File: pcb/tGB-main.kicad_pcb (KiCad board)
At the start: 2 copper layers, 51 x 61 mm, 69 parts, among them J1 DMG-CardEdge, J2 PROG_PORT, Q1 DMG3415U, Q2 HN4A56JU, Q3 2N7002K, U1 TC74LCXR163245FT, U2 TC74LCXR163245FT, U3 ICE40UP5K-SG48ITR, U4 TPS79901DDCR, U5 TPS79901DDCR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

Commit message: rename project
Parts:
- J1: value DMG-CardEdge -> GB-CardEdge; footprint DMG-CardEdge:DMG-CardEdge -> GB-CardEdge:GB-CardEdge
- J2: footprint pinheader:pinheader-10p-sm -> PinHeader:PinHeader-10P-Sidemount

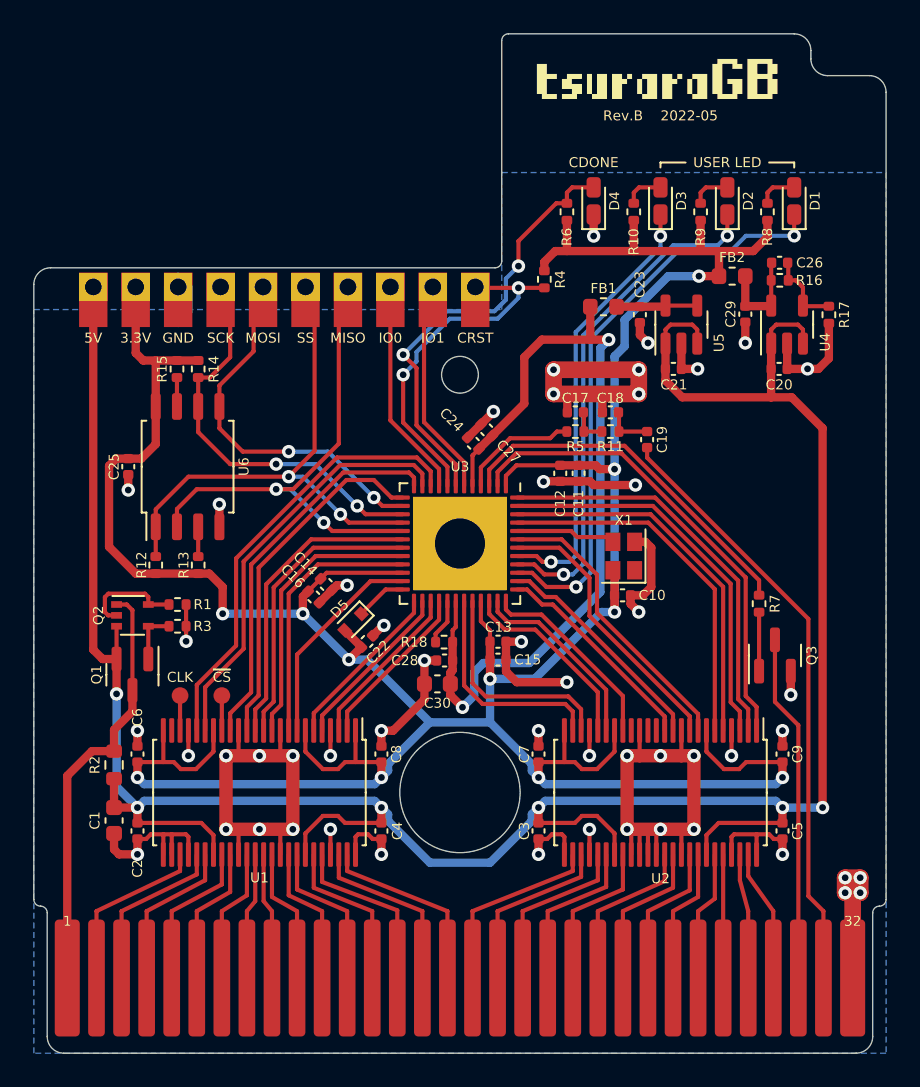
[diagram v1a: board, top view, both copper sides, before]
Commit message: rename project, update pcb
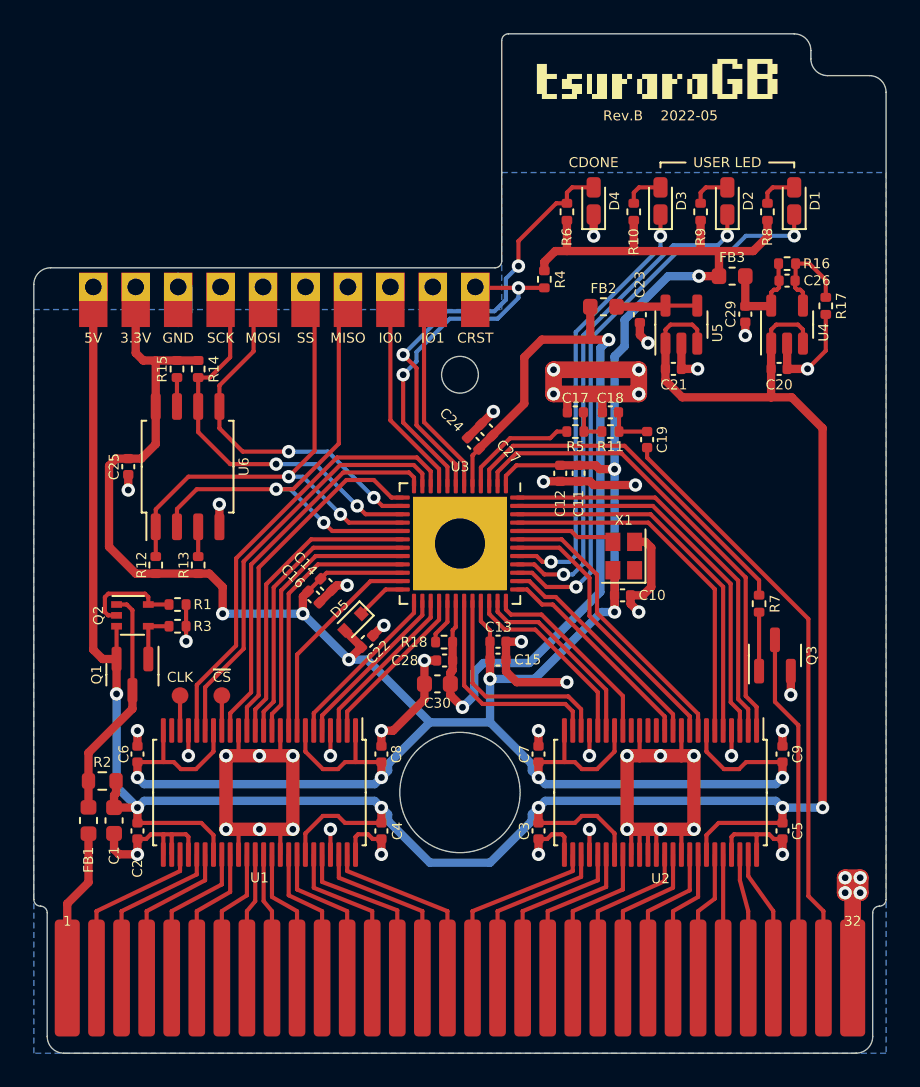
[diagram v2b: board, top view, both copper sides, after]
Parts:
- added FB1: MPZ1608S601ATA00, Inductor_SMD:L_0603_1608Metric, F.Cu at (37.8, 81.6)
- moved R2 1.19 mm to (38.6, 79.2), turned to 0 degrees
- moved C26 1.16 mm to (79.6, 49.3)
- moved R16 1.09 mm to (79.6, 48.2)
- moved R17 0.56 mm to (81.9, 50.8)
- renumbered FB1 to FB2, FB2 to FB3
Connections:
- Q1 pad 3: /VCC -> /VCC0
- Q2 pad 1: /VCC -> /VCC0
- R2 pad 1: /VCC -> /VCC0
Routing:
- net /VCC: track 25.5 -> 9.16 mm
- net /VCC0: track 0.00 -> 14.0 mm
- net Net-(C26-Pad2): track 4.77 -> 6.08 mm

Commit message: update R16,R17 value
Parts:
- R16: value 100kΩ -> 120kΩ
- R17: value 56kΩ -> 68kΩ
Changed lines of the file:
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@@
     (grid_origin 34.5 95.5)
     (pcbplotparams
-      (layerselection 0x00010f0_ffffffff)
+      (layerselection 0x00010fc_ffffffff)
       (disableapertmacros false)
       (usegerberextensions false)
@@
     (fp_line (start -2.5 -3.5) (end 3.5 -3.5) (layer "F.Fab") (width 0.1))
     (fp_line (start -3.5 -2.5) (end -2.5 -3.5) (layer "F.Fab") (width 0.1))
-    (pad "" smd roundrect (at -2.1 -0.7 270) (size 1.13 1.13) (layers "F.Paste") (roundrect_rratio 0.221239))
-    (pad "" smd roundrect (at 2.1 2.1 270) (size 1.13 1.13) (layers "F.Paste") (roundrect_rratio 0.221239))
-    (pad "" smd roundrect (at 0.7 -2.1 270) (size 1.13 1.13) (layers "F.Paste") (roundrect_rratio 0.221239))
-    (pad "" smd roundrect (at -2.1 0.7 270) (size 1.13 1.13) (layers "F.Paste") (roundrect_rratio 0.221239))
-    (pad "" smd roundrect (at -0.7 2.1 270) (size 1.13 1.13) (layers "F.Paste") (roundrect_rratio 0.221239))
-    (pad "" smd roundrect (at -0.7 -2.1 270) (size 1.13 1.13) (layers "F.Paste") (roundrect_rratio 0.221239))
-    (pad "" smd roundrect (at 0.7 2.1 270) (size 1.13 1.13) (layers "F.Paste") (roundrect_rratio 0.221239))
-    (pad "" smd roundrect (at 2.1 0.7 270) (size 1.13 1.13) (layers "F.Paste") (roundrect_rratio 0.221239))
-    (pad "" smd roundrect (at -2.1 2.1 270) (size 1.13 1.13) (layers "F.Paste") (roundrect_rratio 0.221239))
-    (pad "" smd roundrect (at 2.1 -2.1 270) (size 1.13 1.13) (layers "F.Paste") (roundrect_rratio 0.221239))
-    (pad "" smd roundrect (at -2.1 -2.1 270) (size 1.13 1.13) (layers "F.Paste") (roundrect_rratio 0.221239))
-    (pad "" smd roundrect (at 2.1 -0.7 270) (size 1.13 1.13) (layers "F.Paste") (roundrect_rratio 0.221239))
+    (pad "" smd roundrect (at -2.1 -0.7 270) (size 1.13 1.13) (layers "F.Paste") (roundrect_rratio 0.2212389381))
+    (pad "" smd roundrect (at 2.1 2.1 270) (size 1.13 1.13) (layers "F.Paste") (roundrect_rratio 0.2212389381))
+    (pad "" smd roundrect (at 0.7 -2.1 270) (size 1.13 1.13) (layers "F.Paste") (roundrect_rratio 0.2212389381))
+    (pad "" smd roundrect (at -2.1 0.7 270) (size 1.13 1.13) (layers "F.Paste") (roundrect_rratio 0.2212389381))
+    (pad "" smd roundrect (at -0.7 2.1 270) (size 1.13 1.13) (layers "F.Paste") (roundrect_rratio 0.2212389381))
+    (pad "" smd roundrect (at -0.7 -2.1 270) (size 1.13 1.13) (layers "F.Paste") (roundrect_rratio 0.2212389381))
+    (pad "" smd roundrect (at 0.7 2.1 270) (size 1.13 1.13) (layers "F.Paste") (roundrect_rratio 0.2212389381))
+    (pad "" smd roundrect (at 2.1 0.7 270) (size 1.13 1.13) (layers "F.Paste") (roundrect_rratio 0.2212389381))
+    (pad "" smd roundrect (at -2.1 2.1 270) (size 1.13 1.13) (layers "F.Paste") (roundrect_rratio 0.2212389381))
+    (pad "" smd roundrect (at 2.1 -2.1 270) (size 1.13 1.13) (layers "F.Paste") (roundrect_rratio 0.2212389381))
+    (pad "" smd roundrect (at -2.1 -2.1 270) (size 1.13 1.13) (layers "F.Paste") (roundrect_rratio 0.2212389381))
+    (pad "" smd roundrect (at 2.1 -0.7 270) (size 1.13 1.13) (layers "F.Paste") (roundrect_rratio 0.2212389381))
     (pad "1" smd roundrect (at -3.4375 -2.75 270) (size 0.875 0.25) (layers "F.Cu" "F.Paste" "F.Mask") (roundrect_rratio 0.25)
       (net 3 "+3V3") (pinfunction "VCCIO_2") (pintype "power_in"))
@@
       (effects (font (size 0.6 0.6) (thickness 0.12)))
     )
-    (fp_text value "100kΩ" (at 0 1.17) (layer "F.Fab")
+    (fp_text value "120kΩ" (at 0 1.17) (layer "F.Fab")
       (effects (font (size 0.6 0.6) (thickness 0.12)))
     )
@@
       (effects (font (size 0.6 0.6) (thickness 0.12)))
     )
-    (fp_text value "56kΩ" (at 0 1.17 -90) (layer "F.Fab")
-      (effects (font (size 0.6 0.6) (thickness 0.12)))
-    )
+    (fp_text value "68kΩ" (at 0 1.17 -90) (layer "F.Fab")
+      (effects (font (size 0.6 0.6) (thickness 0.12)))
+    )
